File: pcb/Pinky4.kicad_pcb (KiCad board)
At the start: 2 copper layers, 137 x 120 mm, 80 parts, among them J1 MJ-4PP-9, P1 i2c-pin, P2 i2c-pin, SW1 RESET_SW, SW10 SW_PUSH, SW11 SW_PUSH, SW12 SW_PUSH, SW13 SW_PUSH, SW14 SW_PUSH, SW15 SW_PUSH, SW16 SW_PUSH, SW17 SW_PUSH, SW18 SW_PUSH, SW19 SW_PUSH, SW2 SW_PUSH, SW20 SW_PUSH, SW21 SW_PUSH, SW22 SW_PUSH, SW23 SW_PUSH, SW24 SW_PUSH, SW25 SW_PUSH, SW26 SW_PUSH, SW27 SW_PUSH, SW28 SW_PUSH, SW29 SW_PUSH, SW3 SW_PUSH, SW30 SW_PUSH, SW31 SW_PUSH, SW32 SW_PUSH, SW33 SW_PUSH, SW4 SW_PUSH, SW5 SW_PUSH, SW6 SW_PUSH, SW7 SW_PUSH, SW8 SW_PUSH, SW9 SW_PUSH, U1 ProMicro

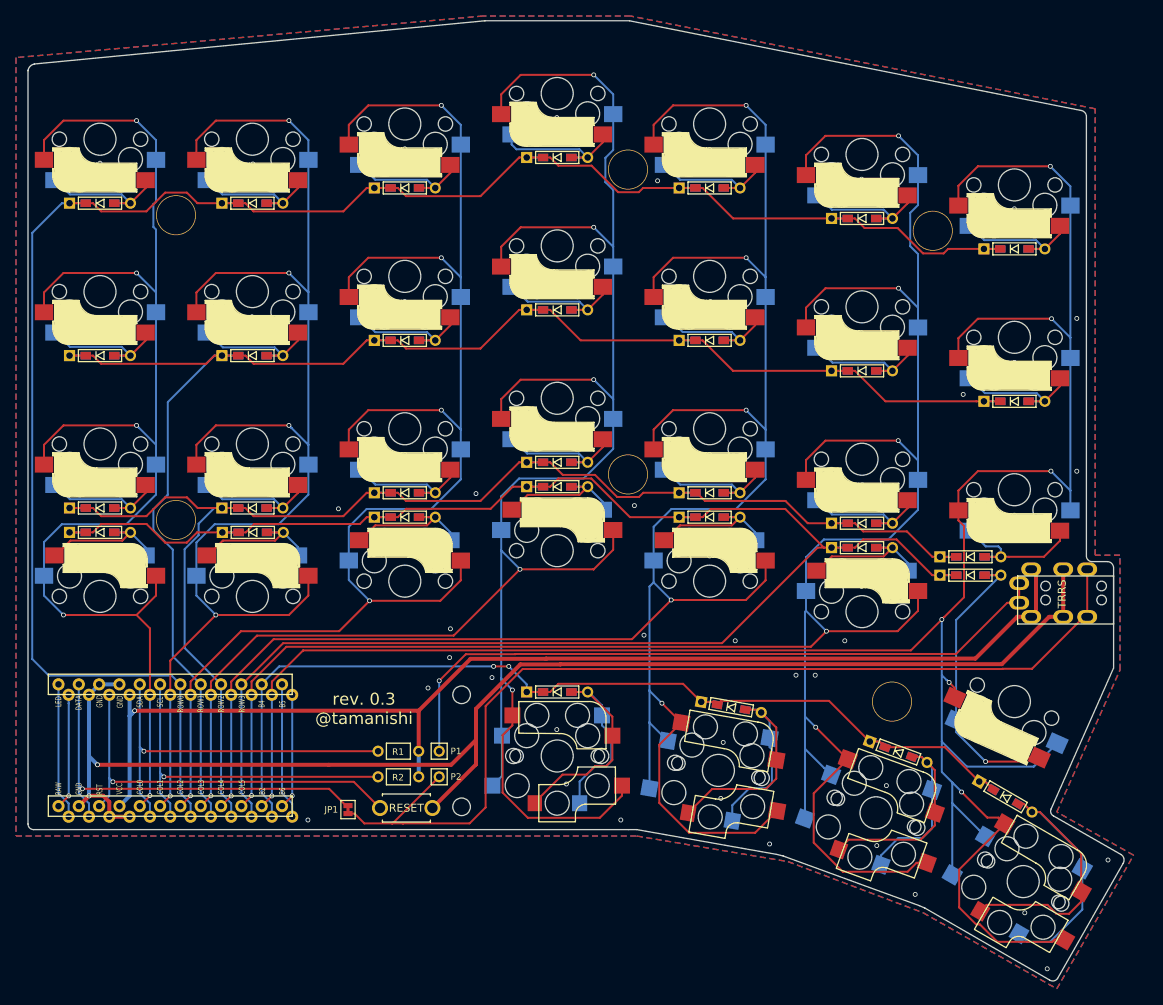
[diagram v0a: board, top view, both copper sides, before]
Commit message: move trrs layout tweaking to another branch
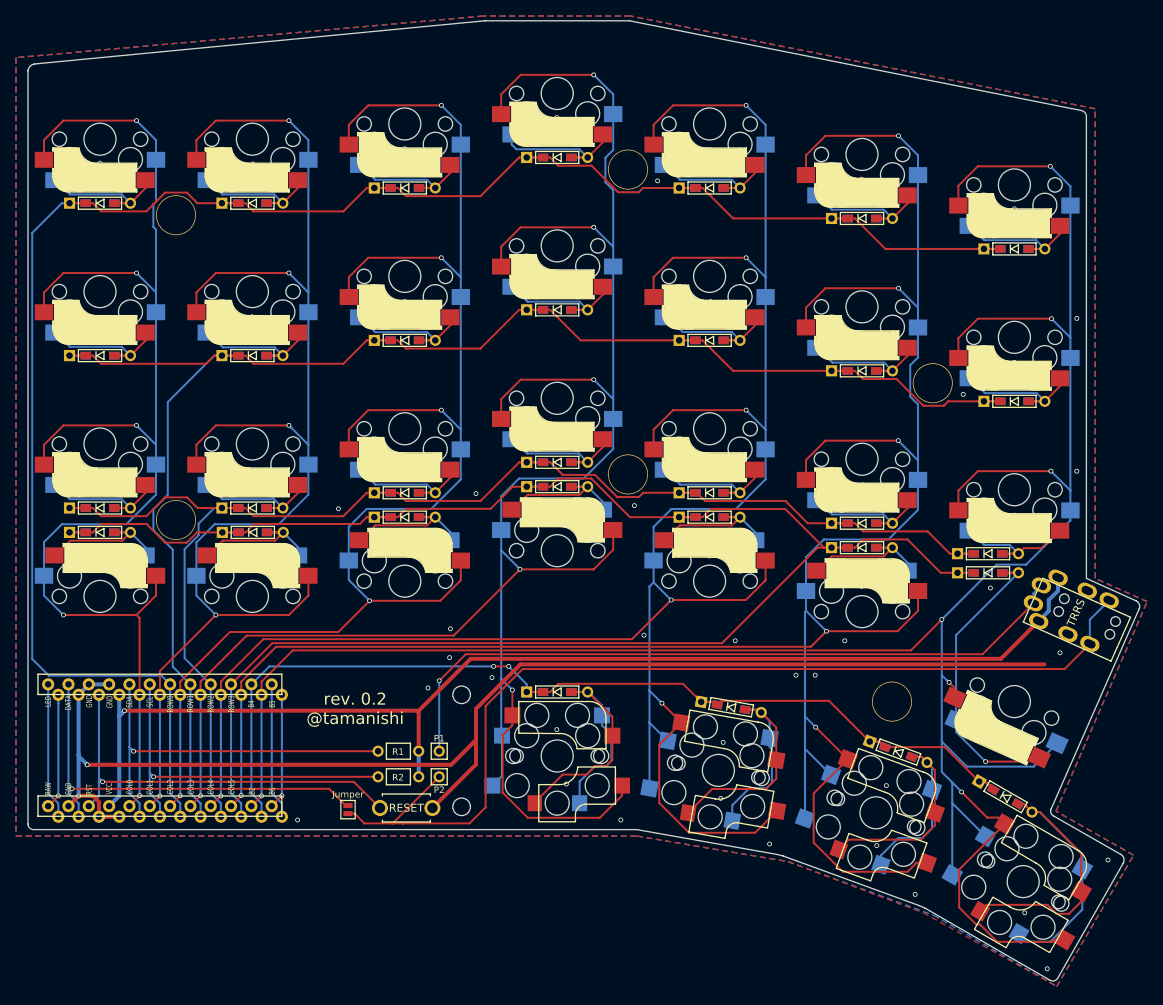
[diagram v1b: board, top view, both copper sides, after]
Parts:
- JP1: value JP -> Jumper; footprint kbd:JP -> kbd:Jumper
- moved Ref** 19.0 mm to (154.1, 80.5)
- moved J1 4.98 mm to (177.6, 112.5), turned to 246 degrees
- moved D30 2.23 mm to (161.0, 101.8)
- moved D31 2.22 mm to (161.0, 104.2)
- moved U1 1.29 mm to (58.0, 125.8)
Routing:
- net GND: track 175.2 -> 165.7 mm, vias 58 -> 60
- net col6: track 309.4 -> 318.1 mm
- net row3: track 233.3 -> 236.8 mm
- net VCC: track 147.1 -> 149.0 mm
- net Net-(J1-PadA): track 87.8 -> 89.7 mm
- net row2: track 179.9 -> 181.7 mm
- net Net-(D30-Pad2): track 19.6 -> 17.9 mm
- net row0: track 238.6 -> 236.8 mm
- net col3: track 266.8 -> 268.1 mm
- net col2: track 184.1 -> 185.4 mm
- net reset: track 49.8 -> 51.1 mm
- net sda: track 47.1 -> 48.4 mm
- net scl: track 44.5 -> 45.8 mm
- net data: track 51.8 -> 53.0 mm
- net col5: track 299.4 -> 300.7 mm
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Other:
- board size 137 x 120 mm -> 139 x 120 mm
- board text added: "rev. 0.2 @tamanishi"
- board text removed: "rev. 0.3 @tamanishi"

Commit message: - readme - rename to Pinky4
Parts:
- JP1: value Jumper -> JP; footprint kbd:Jumper -> kbd:JP
- moved Ref** 19.0 mm to (154.1, 61.5)
- moved J1 4.98 mm to (176.7, 107.6), turned to 270 degrees
- moved D30 2.23 mm to (158.8, 102.2)
- moved D31 2.22 mm to (158.8, 104.5)
- moved U1 1.29 mm to (59.3, 125.8)
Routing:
- net GND: track 165.7 -> 175.2 mm, vias 60 -> 58
- net col6: track 318.1 -> 309.4 mm
- net row3: track 236.8 -> 233.3 mm
- net VCC: track 149.0 -> 147.1 mm
- net Net-(J1-PadA): track 89.7 -> 87.8 mm
- net row2: track 181.7 -> 179.9 mm
- net Net-(D30-Pad2): track 17.9 -> 19.6 mm
- net row0: track 236.8 -> 238.6 mm
- net col3: track 268.1 -> 266.8 mm
- net col2: track 185.4 -> 184.1 mm
- net reset: track 51.1 -> 49.8 mm
- net sda: track 48.4 -> 47.1 mm
- net scl: track 45.8 -> 44.5 mm
- net data: track 53.0 -> 51.8 mm
- net col5: track 300.7 -> 299.4 mm
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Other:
- board size 139 x 120 mm -> 137 x 120 mm
- board text added: "rev. 0.3 @tamanishi"
- board text removed: "rev. 0.2 @tamanishi"
